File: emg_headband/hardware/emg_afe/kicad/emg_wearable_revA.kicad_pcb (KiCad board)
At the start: 2 copper layers, 62.5 x 25.4 mm, 63 parts, among them J1 CH1 (TRS), J3 LiPo pads (protected cell), J6 FLEX ARRAY CH1-3 (FPC 12P 0.5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, J7 USB-C, Q101 AO3401A, U1 ADS1298IPAGR, U2 ESP32-S3-MINI-1-N8, U6 LP5907MFX-3.0, U7 USBLC6-2SC6, U8 MCP73831T-2ACI/OT, U9 AP2112K-3.3TRG1

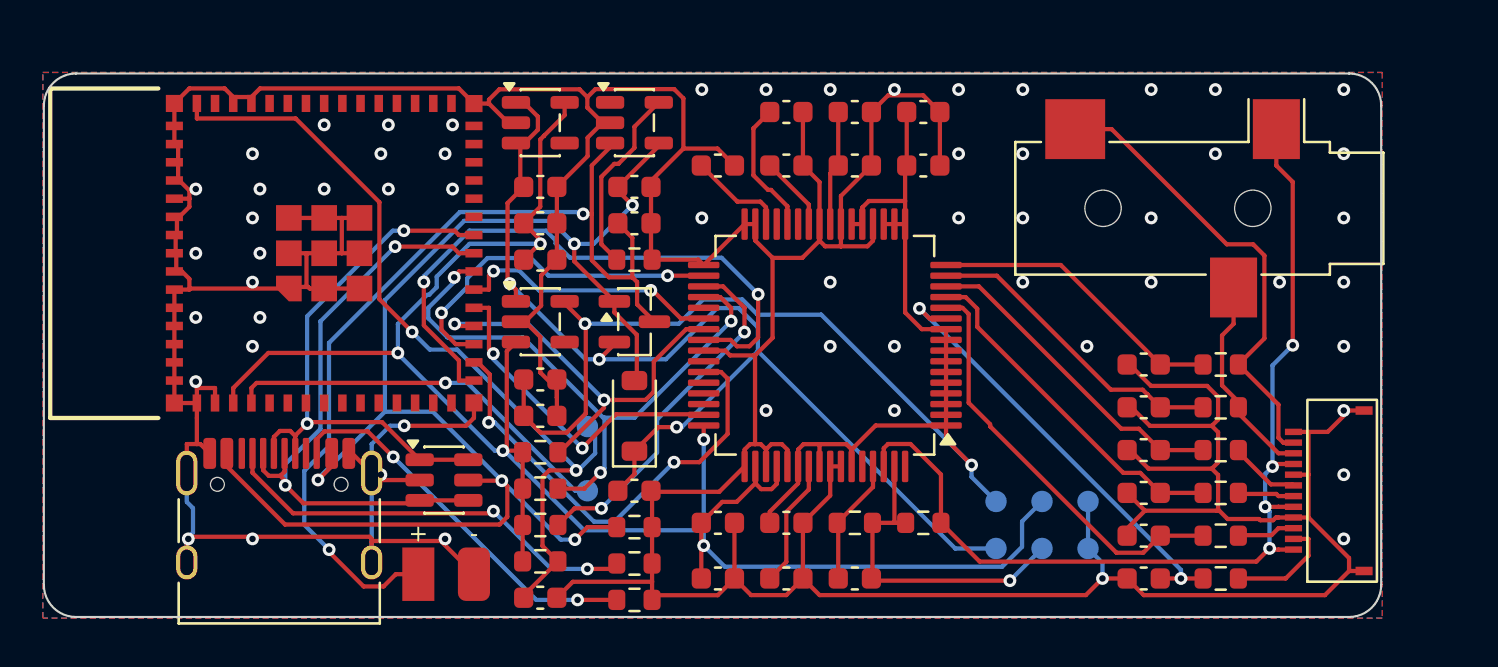
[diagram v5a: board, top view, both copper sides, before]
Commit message: EMG Rev A: power slide switch, battery monitor and charge LED
SW1 (MSK12C02, side lever at the bottom edge) between the battery and
the Q101 system path: off disconnects the cell, USB still powers the
board and charges. VBAT_SYS/2 divider into IO10, MCP73831 STAT LED.
Re-routed, pours and stitching redone; stiffener now covers the switch
and has holes at every peg and USB-C shell tab. ERC 0 errors, DRC 0
errors, 0 unconnected. JLC BOM/CPL (60 parts) and gerbers re-exported
with the rotation/offset corrections.

Co-Authored-By: Claude Opus 5.5 (1M context) <noreply@anthropic.com>
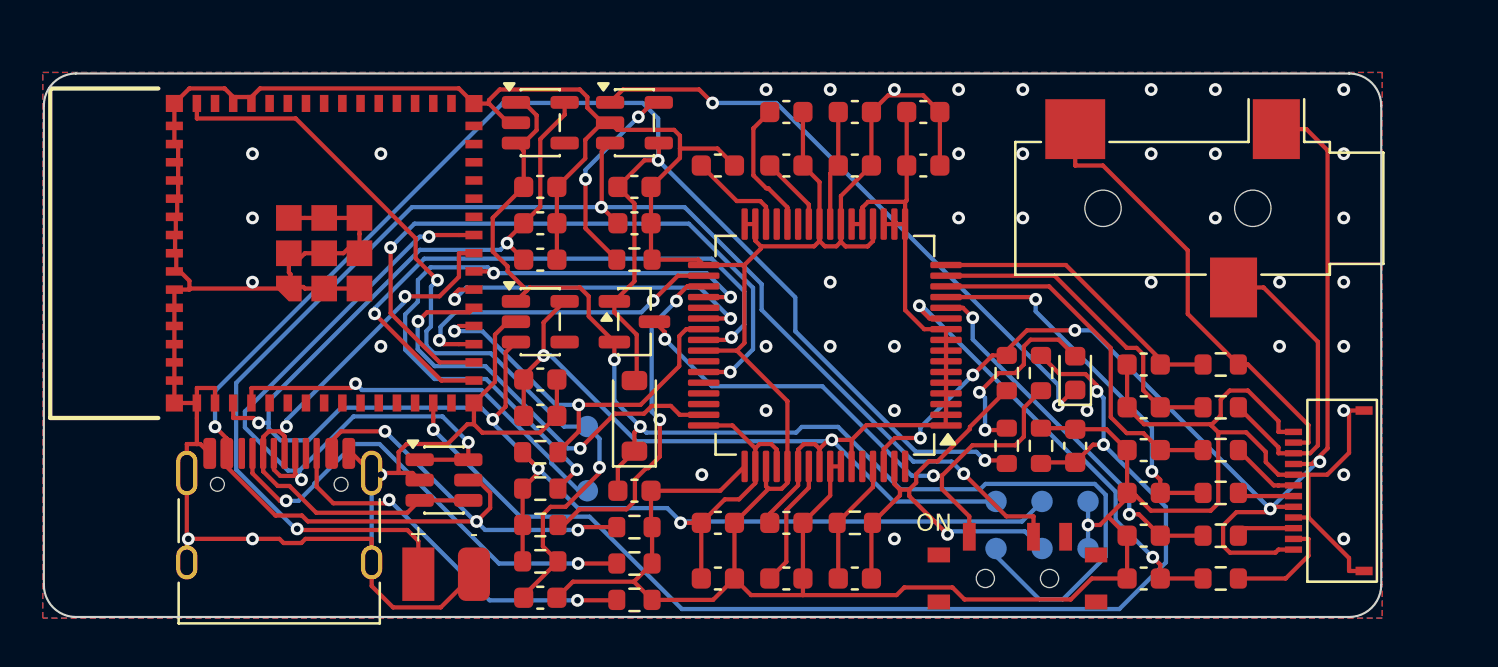
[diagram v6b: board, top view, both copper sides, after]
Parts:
- added C709: 100nF, Capacitor_SMD:C_0603_1608Metric, F.Cu at (98.2, 67.4)
- added D102: CHG red, LED_SMD:LED_0603_1608Metric, F.Cu at (98.2, 64.0)
- added R705: 1M, Resistor_SMD:R_0603_1608Metric, F.Cu at (96.6, 64.0)
- added R706: 1M, Resistor_SMD:R_0603_1608Metric, F.Cu at (96.6, 67.4)
- added R707: 1k, Resistor_SMD:R_0603_1608Metric, F.Cu at (95.0, 67.4)
- added SW1: PWR (MSK12C02), emg_wearable:SW_SPDT_Slide_SHOUHAN_MSK12C02, F.Cu at (95.5, 73.6)
- moved R102 8.01 mm to (95.0, 64.0), turned to 90 degrees
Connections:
- Q101 pad 3: VBAT -> VBAT_SYS
- U2 pad 14: (no net) -> VBAT_SENSE
- U8 pad 1: (no net) -> CHG_STAT
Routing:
- net VBAT_SENSE: track 0.00 -> 55.9 mm, vias 0 -> 3
- net VBUS: track 69.0 -> 100.5 mm, vias 5 -> 6
- net CHG_STAT: track 0.00 -> 29.0 mm, vias 0 -> 2
- net VBAT_SYS: track 0.00 -> 27.1 mm, vias 0 -> 2
- net VBAT: track 44.0 -> 68.0 mm, vias 2 -> 3
- net SPI_MISO: track 21.9 -> 32.2 mm
- net CHG_LED: track 0.00 -> 9.24 mm, vias 0 -> 2
- net RLD_ELEC: track 46.8 -> 55.2 mm, vias 4 -> 5
- net USB_DP: track 26.4 -> 34.5 mm, vias 2 -> 3
- net AGND: track 291.0 -> 283.5 mm, vias 57 -> 43
- net +3V0_A: track 71.1 -> 64.2 mm
- net VSYS: track 52.6 -> 59.2 mm, vias 3 -> 2
- net RLD_OUT: track 15.4 -> 20.7 mm
- net ADS_DRDY: track 15.4 -> 20.5 mm
- net ELEC1_N: track 9.77 -> 14.8 mm
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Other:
- board text added: "ON"
- board text added: "STIFFENER 0.2 mm FR4, back side, 3 areas (outlines); circles = holes in the stiffener for pegs and USB-C shell tabs."
- board text removed: "STIFFENER 0.2 mm FR4, back side, 3 areas. Bend zones: power column and input RC block."

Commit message: J6 footprint: mounting tabs at 2.5-3.3 mm per the Hirose land pattern
The FH34SRJ 3.3 mm dimension runs from the outer edge of the signal pads
to the outer edge of the mounting tabs; the tabs were 0.8 mm too far
toward the connector front. Gerbers re-exported; DRC 0 errors.

Co-Authored-By: Claude Opus 5.5 (1M context) <noreply@anthropic.com>
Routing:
- net AGND: vias 43 -> 42
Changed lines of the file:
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@@
 		(layer "F.Cu")
 		(at 108 69.5 90)
-		(descr "Hirose FH34SRJ-12S-0.5SH(50), 12 contacts, 0.5 mm pitch, 1.0 mm tall, back-flip ZIF, top and bottom contact. Land pattern from the Hirose datasheet (Aug 2019, p.4): signal pads 0.3 x 0.8, mounting pads 0.4 x 0.8, E=7.1, F=7.9, 3.3 from signal pad edge to mounting pad edge. FPC inserts from the mounting-tab side (+Y); the signal pads are at the back (actuator side). Check against the datasheet before ordering.")
+		(descr "Hirose FH34SRJ-12S-0.5SH(50), 12 contacts, 0.5 mm pitch, 1.0 mm tall, back-flip ZIF, top and bottom contact. Land pattern from the Hirose datasheet (Aug 2019, p.4): signal pads 0.3 x 0.8, mounting pads 0.4 x 0.8, E=7.1, F=7.9, 3.3 from the outer edge of the signal pads to the outer edge of the mounting pads (tabs at 2.5-3.3). FPC inserts from the mounting-tab side (+Y); the signal pads are at the back (actuator side). Check against the datasheet before ordering.")
 		(tags "FPC FFC Hirose FH34SRJ 0.5mm 12pin")
 		(property "Reference" "J6"
@@
 		(fp_rect
 			(start -4.25 1.05)
-			(end 4.25 4.3)
+			(end 4.25 3.55)
 			(stroke
 				(width 0.12)
@@
 		(fp_rect
 			(start -4.55 -0.3)
-			(end 4.55 4.6)
+			(end 4.55 3.6)
 			(stroke
 				(width 0.05)
@@
 		(fp_rect
 			(start -4 0.75)
-			(end 4 4.05)
+			(end 4 3.4)
 			(stroke
 				(width 0.1)
@@
 		)
 		(pad "MP" smd rect
-			(at -3.75 3.7 90)
+			(at -3.75 2.9 90)
 			(size 0.4 0.8)
 			(layers "F.Cu" "F.Mask" "F.Paste")
@@
 		)
 		(pad "MP" smd rect
-			(at 3.75 3.7 90)
+			(at 3.75 2.9 90)
 			(size 0.4 0.8)
 			(layers "F.Cu" "F.Mask" "F.Paste")
@@
 		(size 0.6)
 		(drill 0.3)
-		(layers "F.Cu" "B.Cu")
-		(net "AGND")
-	)
-	(via
-		(at 110.75 65.75)
-		(size 0.6)
-		(drill 0.3)
